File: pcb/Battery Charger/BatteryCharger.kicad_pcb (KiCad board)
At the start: 2 copper layers, 6 parts, among them U2 MCP73831-2-OT

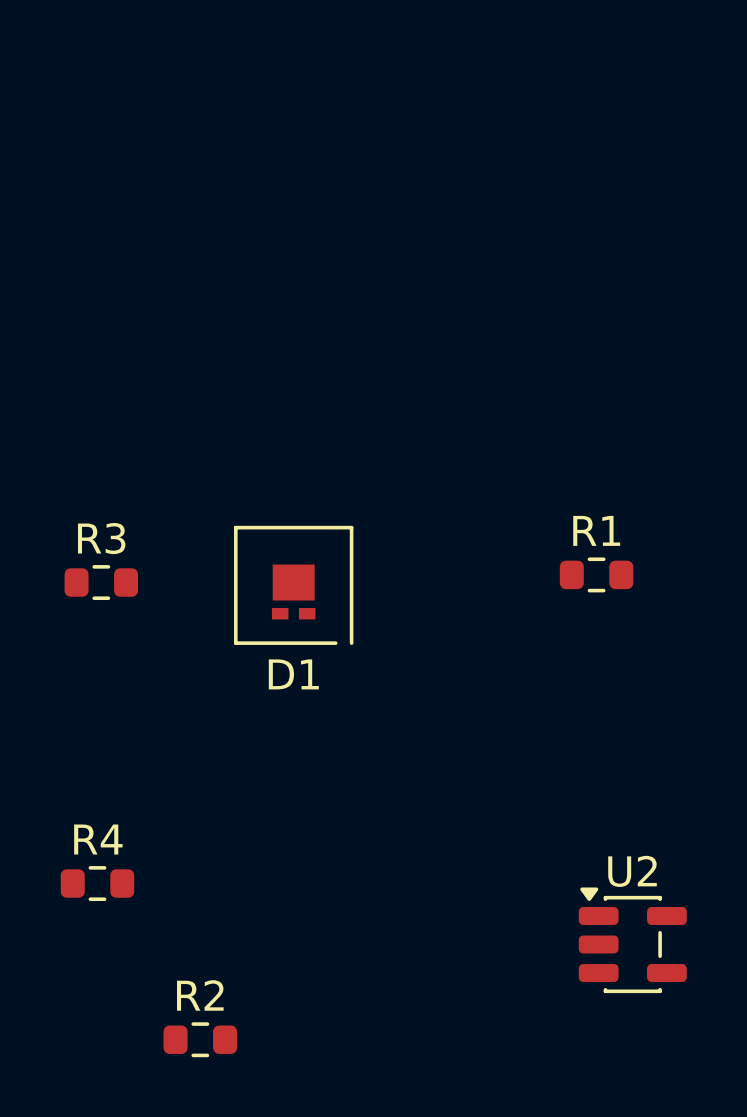
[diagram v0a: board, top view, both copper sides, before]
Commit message: I added the 2 extra components to the battery regulator
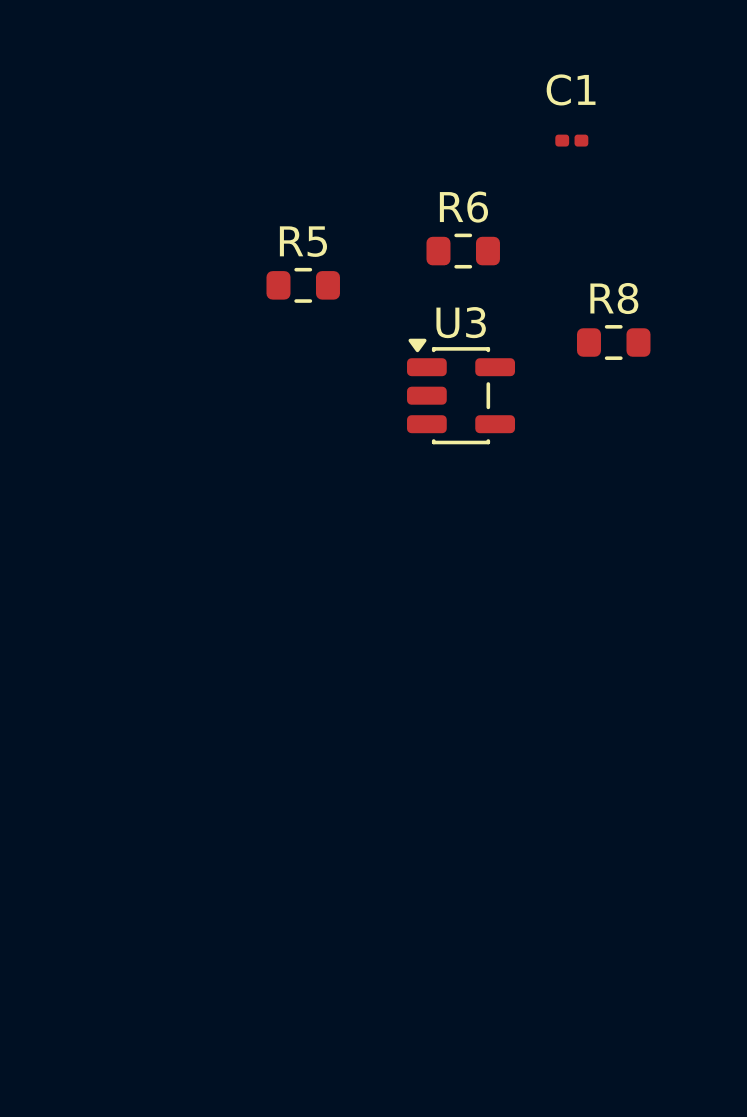
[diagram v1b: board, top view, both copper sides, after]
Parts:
- removed D1: LED_Dual_AAK, LED_SMD:LED-L1T2_LUMILEDS
- removed R1: 2k, Resistor_SMD:R_0603_1608Metric
- removed R2: 470, Resistor_SMD:R_0603_1608Metric
- removed R3: 330, Resistor_SMD:R_0603_1608Metric
- removed R4: 1k, Resistor_SMD:R_0603_1608Metric
- removed U2: MCP73831-2-OT, Package_TO_SOT_SMD:SOT-23-5
- added C1: C_0201_0603Metric, Capacitor_SMD:C_0201_0603Metric, F.Cu at (157.9, 80.9)
- added R5: 500, Resistor_SMD:R_0603_1608Metric, F.Cu at (148.9, 85.7)
- added R6: 2k, Resistor_SMD:R_0603_1608Metric, F.Cu at (154.2, 84.6)
- added R8: 225, Resistor_SMD:R_0603_1608Metric, F.Cu at (159.3, 87.6)
- added U3: MCP73831-2-OT, Package_TO_SOT_SMD:SOT-23-5, F.Cu at (154.2, 89.4)

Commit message: i just made some changes
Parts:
- added B+1: B+, TestPoint:TestPoint_THTPad_D1.0mm_Drill0.5mm, F.Cu at (194.5, 56.3)
- added B-1: B-, TestPoint:TestPoint_THTPad_D1.0mm_Drill0.5mm, F.Cu at (198.9, 56.3)
- added C2: 12, Capacitor_SMD:C_0805_2012Metric, F.Cu at (192.8, 90.4)
- added C3: 4.7, Capacitor_SMD:C_0805_2012Metric, F.Cu at (189.2, 86.6)
- added C4: 4.7, Capacitor_SMD:C_0805_2012Metric, F.Cu at (191.9, 57.4)
- added C5: 0.1, Capacitor_SMD:C_0603_1608Metric, F.Cu at (188.7, 77.4)
- added D1: LED, LED_SMD:LED_0805_2012Metric, F.Cu at (185.3, 62.4)
- added D2: SS14, Diode_SMD:D_SMA, F.Cu at (199.1, 84.8)
- added D3: SS14, Diode_SMD:D_SMA, F.Cu at (186.3, 90.3)
- added D4: SS14, Diode_SMD:D_SMA, F.Cu at (193.9, 84.0)
- added D5: SS14, Diode_SMD:D_SMA, F.Cu at (187.1, 59.5)
- added GND1: B-, TestPoint:TestPoint_THTPad_D1.0mm_Drill0.5mm, F.Cu at (191.6, 96.4)
- added L1: 22, Inductor_SMD:L_Bourns-SRN6028, F.Cu at (197.6, 63.0)
- added PS1: ME2108A33P, fs8205afootprint:ME2108A33P, F.Cu at (199.1, 91.8)
- added Pogo+1: Pogo+, TestPoint:TestPoint_THTPad_D1.0mm_Drill0.5mm, F.Cu at (187.9, 96.5)
- added Q1: FS8205A, fs8205afootprint:FS8205A, F.Cu at (188.0, 68.2)
- added R7: 1k, Resistor_SMD:R_0603_1608Metric, F.Cu at (147.4, 78.5)
- added U1: DW01A, Package_TO_SOT_SMD:SOT-23-6, F.Cu at (197.8, 73.0)
- added VBUS1: Output 5V, TestPoint:TestPoint_THTPad_D1.0mm_Drill0.5mm, F.Cu at (184.3, 96.4)
- C1: value C_0201_0603Metric -> 12; footprint Capacitor_SMD:C_0201_0603Metric -> Capacitor_SMD:C_0805_2012Metric
- R5: value 500 -> 470
- R8: value 225 -> 100
- U3: value MCP73831-2-OT -> MCP73831
- moved U3 45.1 mm to (191.0, 63.4), turned to 90 degrees
- moved R5 42.0 mm to (185.2, 64.5), turned to 180 degrees
- moved C1 38.4 mm to (195.1, 90.4), turned to -90 degrees
- moved R8 31.5 mm to (190.2, 81.8), turned to 180 degrees
- moved R6 27.3 mm to (179.2, 73.5), turned to 180 degrees
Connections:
- C1 pad 1: (no net) -> Net-(D2-K)
- C1 pad 2: (no net) -> GND
- R8 pad 1: unconnected-(R8-Pad1) -> Net-(D4-A)
- U3 pad 3: unconnected-(C3-Pad1) -> Net-(D4-A)
- U3 pad 4: unconnected-(C4-Pad1) -> Net-(D1-A)
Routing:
- net Net-(D2-A): track 0.00 -> 40.6 mm
- net Net-(D2-K): track 0.00 -> 22.5 mm
- net Net-(D1-A): track 0.00 -> 17.8 mm
- net Net-(U1-GND): track 0.00 -> 16.0 mm
- net Net-(D4-A): track 0.00 -> 14.9 mm
- net Net-(U1-OC): track 0.00 -> 14.0 mm
- net Net-(U1-OD): track 0.00 -> 7.76 mm
- net Net-(D3-K): track 0.00 -> 6.10 mm
- added copper zone on B.Cu, net GND
- added copper zone on F.Cu, net GND
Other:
- board outline added: 153.1 x 58.3 mm

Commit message: Rough Draft FINISHED
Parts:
- moved Pogo 40.3 mm to (190.2, 56.3)
- moved R7 38.6 mm to (185.4, 71.5), turned to 180 degrees
- moved VBUS 9.47 mm to (186.6, 87.2)
- moved GND 9.33 mm to (190.8, 87.1)
- moved C3 9.00 mm to (187.3, 77.8)
- moved D2 8.61 mm to (199.4, 76.2)
- moved C1 8.23 mm to (195.8, 82.2)
- moved C2 8.23 mm to (193.6, 82.2)
- moved D3 8.23 mm to (187.1, 82.1)
- moved PS1 8.23 mm to (199.8, 83.6)
- moved D4 7.92 mm to (195.3, 76.2)
- moved R6 6.19 mm to (185.3, 74.4)
- moved C5 5.67 mm to (191.8, 72.7)
- moved R8 4.94 mm to (190.9, 76.9)
- moved U1 3.75 mm to (195.2, 70.3)
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- renumbered B+1 to B+, B-1 to B-, GND1 to GND, Pogo+1 to Pogo, VBUS1 to VBUS
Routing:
- net Net-(D2-A): track 40.6 -> 19.3 mm, vias 0 -> 2
- net Net-(U1-VCC): track 0.00 -> 21.1 mm
- net Net-(U1-GND): track 16.0 -> 34.5 mm, vias 0 -> 2
- net Net-(D4-A): track 14.9 -> 33.2 mm
- net Net-(U3-PROG): track 0.00 -> 17.9 mm
- net GND: track 0.00 -> 14.1 mm, vias 0 -> 2
- net Net-(U1-CS): track 0.00 -> 8.30 mm
- net Net-(U3-STAT): track 0.00 -> 4.12 mm
- net Net-(D2-K): track 22.5 -> 25.2 mm
- net Net-(U1-OD): track 7.76 -> 5.16 mm, vias 0 -> 2
- net Net-(D1-K): track 0.00 -> 2.11 mm
- net Net-(U1-OC): track 14.0 -> 16.0 mm, vias 0 -> 2
- net Net-(D1-A): track 17.8 -> 16.2 mm
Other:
- board size 153.1 x 58.3 mm -> 20 x 37.4 mm

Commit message: charger has been finished final draft
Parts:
- moved PS1 3.73 mm to (198.7, 87.2), turned to 180 degrees
- moved Pogo 0.70 mm to (189.6, 56.0)
- moved C4 0.65 mm to (193.2, 57.8)
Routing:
- net Net-(D3-K): track 5.72 -> 29.6 mm
- net Net-(D2-K): track 25.2 -> 32.8 mm
- net Net-(D2-A): track 19.3 -> 24.3 mm
- net GND: track 14.1 -> 18.9 mm, vias 2 -> 4
- net Net-(D4-A): track 33.2 -> 36.8 mm
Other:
- board size 20 x 37.4 mm -> 20.1 x 37.4 mm
